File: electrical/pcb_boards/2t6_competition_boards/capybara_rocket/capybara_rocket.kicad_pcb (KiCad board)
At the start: 4 copper layers, 160 x 65 mm, 121 parts, among them J1 3.6V Battery, J10 Elevator, J11 SparkFun MAX-M10S, J12 Aileron 1, J13 Aileron 2, J14 Ground Camera, J15 Payload Camera, J16 DC Motor, J2 1.2V Battery, J3 3.6V Switch, J4 1.2V Switch, J5 LED, J6 NC, J7 CC, J8 VL53L1-SATEL, J9 Egg, Q1 SI4435DDY, Q2 SI4435DDY, U1 DS1307+, U10 TPS3839, U11 MP3414, U12 SN74LVC1G04, U13 MCP1640, U14 TPS3839, U15 STM32 NUCLEO-G431KB, U16 SN74AUP1G04, U17 SparkFun XBee Explorer, U2 Adafruit BNO085, U3 TLC555, U4 EEPROM, U5 LTC3536, U6 LTC3536, U7 Adafruit BMP581, U8 DRV8212, U9 INA219, Y1 AB38T-32.768KHZ

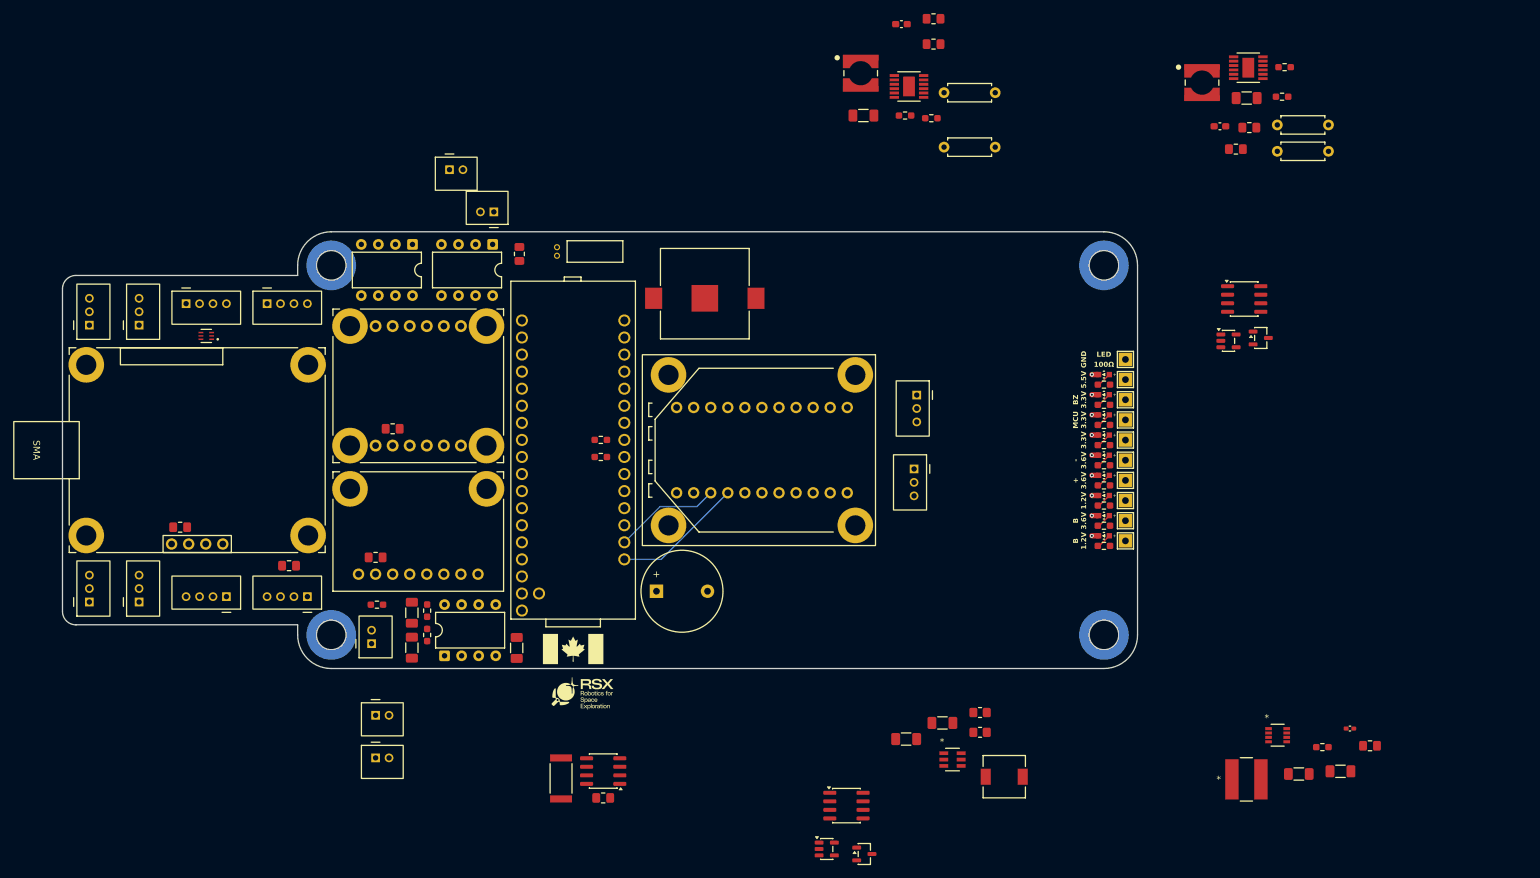
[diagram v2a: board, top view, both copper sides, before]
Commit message: Completed layout for CPL PCB
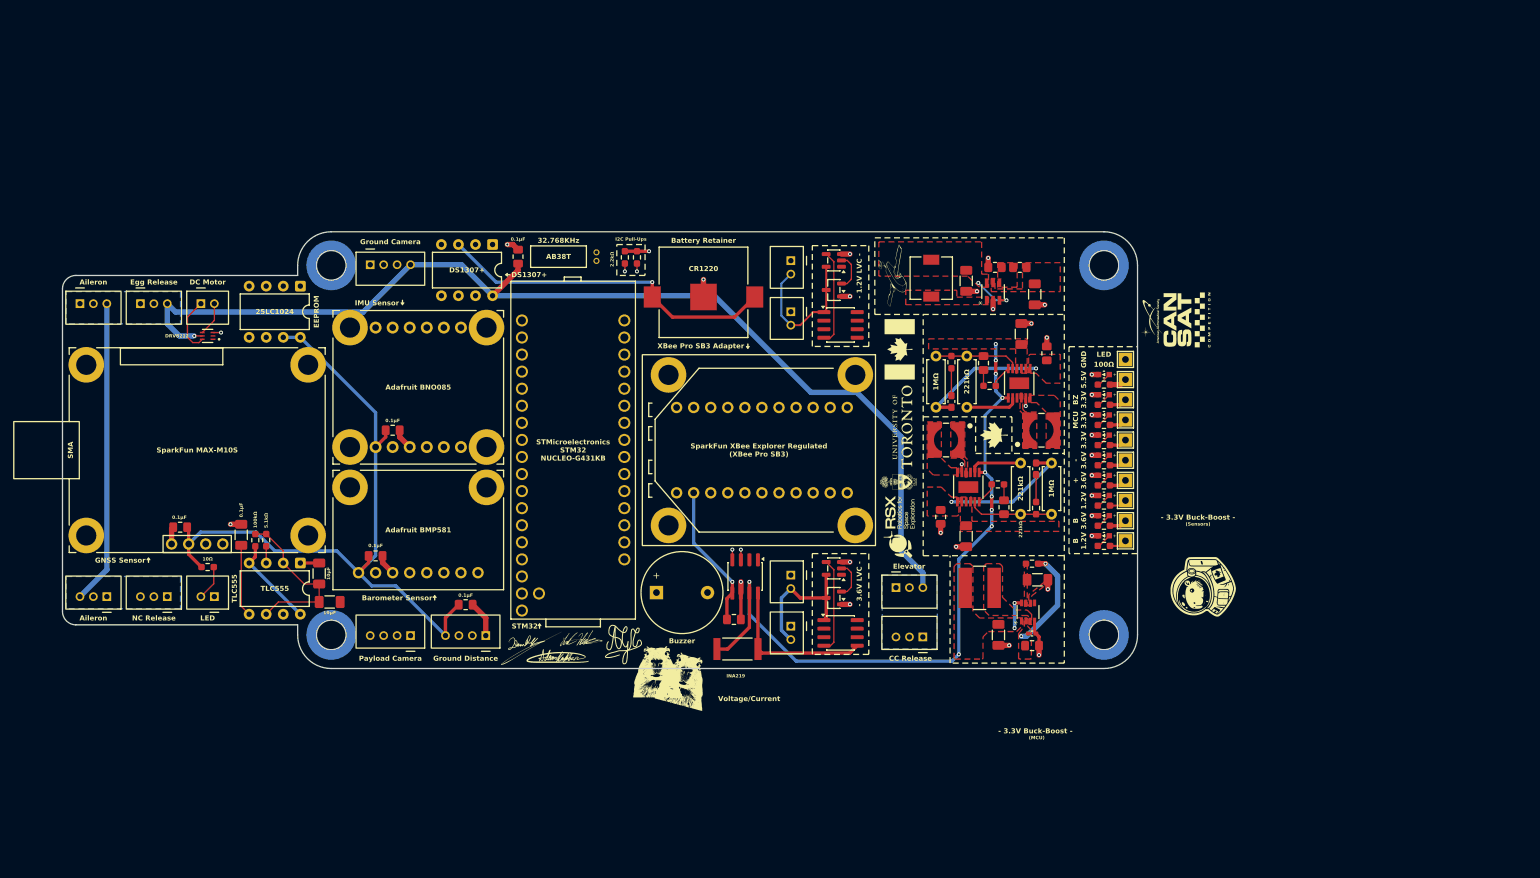
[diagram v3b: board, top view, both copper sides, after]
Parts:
- added ?: , clipboard:8695c1bd-c6c1-4d98-8ee2-76d7a5019fa7, F.Cu at (125.4, 121.6)
- added ?: , clipboard:8695c1bd-c6c1-4d98-8ee2-76d7a5019fa7, F.Cu at (135.9, 73.9)
- added ?: , clipboard:8695c1bd-c6c1-4d98-8ee2-76d7a5019fa7, F.Cu at (141.0, 125.8)
- added ?: , clipboard:8695c1bd-c6c1-4d98-8ee2-76d7a5019fa7, F.Cu at (172.0, 84.9)
- added ?: , clipboard:8695c1bd-c6c1-4d98-8ee2-76d7a5019fa7, F.Cu at (82.8, 116.0)
- added ?: , clipboard:8695c1bd-c6c1-4d98-8ee2-76d7a5019fa7, F.Cu at (120.6, 78.4)
- added G***: LOGO, LOGO, F.Cu at (139.8, 129.4)
- added G***: LOGO, LOGO, F.Cu at (153.6, 129.0)
- added G***: LOGO, RSX_CanSat_Graphics:maple_leaf, F.Cu at (208.6, 97.8)
- added G***: LOGO, RSX_CanSat_Graphics:capybara_astronaut_2, B.Cu at (93.6, 64.6)
- added G***: LOGO, CAN-RGX:uoft, F.Cu at (194.6, 98.2)
- added G***: LOGO, LOGO, F.Cu at (143.6, 130.8)
- added G***: LOGO, RSX_CanSat_Graphics:capybara, F.Cu at (162.7, 133.5)
- added G***: LOGO, RSX_CanSat_Graphics:capybara, F.Cu at (158.5, 132.3)
- added G***: LOGO, RSX_CanSat_Graphics:capybara_astronaut_2, F.Cu at (239.8, 120.2)
- added G***: LOGO, LOGO, F.Cu at (147.5, 127.5)
- added G***: LOGO, RSX_CanSat_Graphics:cansat_logo_2, F.Cu at (235.7, 80.6)
- added G***: LOGO, LOGO, F.Cu at (193.2, 74.0)
- J16: footprint RSX_CanSat_Custom_KiCad_Footprints:J_Wurth_WR-WTB_62000411622 -> RSX_CanSat_Custom_KiCad_Footprints:J_Wurth_WR-WTB_62000211622
- moved J2 91.6 mm to (178.4, 71.8), turned to -90 degrees
- moved J4 90.7 mm to (178.4, 79.4), turned to -90 degrees
- moved U16 87.6 mm to (184.8, 71.8), turned to 180 degrees
- moved J1 84.8 mm to (178.4, 126.2), turned to -90 degrees
- moved U14 84.1 mm to (184.8, 76.2), turned to 180 degrees
- moved Q1 78.0 mm to (185.8, 127.2)
- moved C7 77.4 mm to (204.5, 112.8), turned to -90 degrees
- moved R5 75.3 mm to (209.2, 105.1)
- moved U6 75.0 mm to (204.8, 105.5), turned to -90 degrees
- moved L4 75.0 mm to (199.3, 74.4), turned to 90 degrees
- moved U10 74.4 mm to (184.8, 122.0), turned to 180 degrees
- moved C17 73.9 mm to (200.7, 109.9), turned to 90 degrees
- moved Q2 71.5 mm to (185.8, 81.4)
- moved R8 71.3 mm to (214.9, 108.6), turned to 90 degrees
- moved U13 69.9 mm to (208.5, 76.4), turned to 90 degrees
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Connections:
- J16 pad 1: GND -> DC_PWM_1
- J16 pad 2: DC_PWM_1 -> DC_PWM_2
- J8 pad 2: SCL -> SDA
- J8 pad 3: SDA -> SCL
- U5 pad 8: unconnected-(U5-VIN_2-Pad8) -> 3.6V-
- U6 pad 8: unconnected-(U6-VIN_2-Pad8) -> 3.6V-
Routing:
- net 5.5V: track 0.00 -> 225.5 mm, vias 0 -> 3
- net 3.3V: track 0.00 -> 154.4 mm, vias 0 -> 3
- net 3.6V-: track 0.00 -> 111.5 mm, vias 0 -> 12
- net GND: track 9.00 -> 82.0 mm, vias 9 -> 31
- net SDA: track 0.00 -> 61.5 mm, vias 0 -> 2
- net SCL: track 0.00 -> 60.7 mm, vias 0 -> 2
- net Net-(U1-VBAT): track 0.00 -> 51.1 mm, vias 0 -> 1
- net AILERON: track 0.00 -> 46.4 mm
- net 3.6V+: track 0.00 -> 26.4 mm
- net Net-(U3-THRES): track 0.00 -> 24.9 mm
- net 3.6V B: track 0.00 -> 24.1 mm
- net 1.2V B: track 0.00 -> 24.0 mm
- net 3.3V MCU: track 0.00 -> 22.2 mm, vias 0 -> 1
- net X2: track 0.00 -> 19.0 mm
- net 3.3V BZ: track 0.00 -> 16.2 mm
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- added copper zone on F.Cu, net 1.2V
- added copper zone on F.Cu, net 3.3V
- added copper zone on F.Cu, net 3.3V BZ
- added copper zone on F.Cu, net 3.3V MCU
- added copper zone on F.Cu, net 3.6V-
- added copper zone on B.Cu, net 5.5V
- added copper zone on F.Cu, net 5.5V
- added copper zone on F.Cu, net GND
- added copper zone on F.Cu, net Net-(U11-FB)
- added copper zone on F.Cu, net Net-(U11-SW)
- added copper zone on F.Cu, net Net-(U13-SW)
- added copper zone on F.Cu, net Net-(U13-VFB)
- added copper zone on F.Cu, net Net-(U5-SW1)
- added copper zone on F.Cu, net Net-(U5-SW2)
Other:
- board text added: "(+)"
- board text added: "(MCU)"
- board text added: "(Sensors)"
- board text added: "- 1.2V LVC -"
- board text added: "- 3.3V Buck-Boost -"
- board text added: "- 3.6V LVC -"
- board text added: "0.1μF"
- board text added: "100kΩ"
- board text added: "10Ω"
- board text added: "10μF"
- board text added: "1MΩ"
- board text added: "2.2kΩ"
- board text added: "221kΩ"
- board text added: "25LC1024"
- board text added: "32.768KHz"
- board text added: "3Vo"
- board text added: "5.1kΩ"
- board text added: "AB38T"
- board text added: "Adafruit BMP581"
- board text added: "Adafruit BNO085"
- board text added: "Adam Kabbara Arthur Goetzke-Coburn Daniel Yu Luke Watson Angelique Liao Ada Selcuk Yulin Lin Jingshu Zhu Vincent Jia Wareesha Qureshi Parth Bhasin John Yfantis Nathan Xia Gianluca Ceccacci Berk Yilmaz Remi Zhang June 4-7, 2026 Monterey, Virginia United States"
- board text added: "Aileron"
- board text added: "BT"
- board text added: "Barometer Sensor"
- board text added: "Battery Retainer"
- board text added: "Buzzer"
- board text added: "CC Release"
- board text added: "CONT"
- board text added: "CR1220"
- board text added: "CS"
- board text added: "DC Motor"
- board text added: "DI"
- board text added: "DISCH"
- board text added: "DRV8212"
- board text added: "DS1307+"
- board text added: "EEPROM"
- board text added: "EGG_REL"
- board text added: "Egg Release"
- board text added: "Elevator"
- board text added: "GNSS Sensor"
- board text added: "Ground Camera"
- board text added: "Ground Distance"
- board text added: "HOLD"
- board text added: "I2C Pull-Ups"
- board text added: "IMU Sensor"
- board text added: "INA219"
- board text added: "INT"
- board text added: "MISO"
- board text added: "MOSI"
- board text added: "NC Release"
- board text added: "OUT"
- board text added: "P0"
- board text added: "P1"
- board text added: "Payload Camera"
- board text added: "RST"
- board text added: "SCLK"
- board text added: "SDO"
- board text added: "STM32"
- board text added: "STMicroelectronics STM32 NUCLEO-G431KB"
- board text added: "SparkFun MAX-M10S"
- board text added: "SparkFun XBee Explorer Regulated (XBee Pro SB3)"
- board text added: "THRES"
- board text added: "TLC555"
- board text added: "TRIG"
- board text added: "VCC"
- board text added: "VIN"
- board text added: "VSS"
- board text added: "Voltage/Current"
- board text added: "WP"
- board text added: "X1"
- board text added: "X2"
- board text added: "XBee Pro SB3 Adapter"
- board text removed: "Adam Kabbara Arthur Goetzke-Coburn Daniel Yu Luke Watson Angelique Liao Ada Selcuk Yulin Lin Jingshu Zhu Vincent Jia Wareesha Qureshi Parth Bhasin John Yfantis Nathan Xia Gianluca Ceccacci Berk Yilmaz Remi Zhang"
- board text removed: "EGG"

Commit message: Left side of the board done :)
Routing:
- net Net-(BZ1-+): track 2.49 -> 66.5 mm, vias 0 -> 2
- net PG_CAM_OUT: track 0.00 -> 8.26 mm, vias 0 -> 1
- net PG_CAM_IN: track 0.00 -> 5.93 mm, vias 0 -> 1
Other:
- board text added: "VBAT"
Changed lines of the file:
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@@
+		)
+	)
+	(gr_text "OUT"
+		(at 131.47 78.2 90)
+		(layer "B.SilkS")
+		(effects
+			(font
+				(size 0.75 0.75)
+				(thickness 0.125)
+				(bold yes)
+			)
+			(justify left mirror)
+		)
+	)
+	(gr_text "VBAT"
+		(at 128.93 70.6 90)
+		(layer "B.SilkS")
+		(effects
+			(font
+				(size 0.75 0.75)
+				(thickness 0.125)
+				(bold yes)
+			)
+			(justify left mirror)
 		)
 	)
@@
 		)
 	)
+	(gr_text "SCL"
+		(at 128.93 78.2 90)
+		(layer "B.SilkS")
+		(effects
+			(font
+				(size 0.75 0.75)
+				(thickness 0.125)
+				(bold yes)
+			)
+			(justify left mirror)
+		)
+	)
 	(gr_text "WP"
 		(at 100.32 76.8 90)
@@
 		)
 	)
+	(gr_text "X2"
+		(at 131.47 70.6 90)
+		(layer "B.SilkS")
+		(effects
+			(font
+				(size 0.75 0.75)
+				(thickness 0.125)
+				(bold yes)
+			)
+			(justify left mirror)
+		)
+	)
 	(gr_text "5.5V"
 		(at 115.8 126.6 90)
@@
 		)
 	)
+	(gr_text "GND"
+		(at 126.39 70.6 90)
+		(layer "B.SilkS")
+		(effects
+			(font
+				(size 0.75 0.75)
+				(thickness 0.125)
+				(bold yes)
+			)
+			(justify left mirror)
+		)
+	)
 	(gr_text "MCU\n3.3V"
 		(at 225.6 95.5 90)
@@
 		)
 	)
+	(gr_text "VCC"
+		(at 136 77 90)
+		(layer "B.SilkS")
+		(effects
+			(font
+				(size 0.75 0.75)
+				(thickness 0.125)
+				(bold yes)
+			)
+			(justify mirror)
+		)
+	)
 	(gr_text "SDA"
 		(at 126.76 98.1 90)
@@
 		)
 	)
+	(gr_text "X1"
+		(at 134.01 70.6 90)
+		(layer "B.SilkS")
+		(effects
+			(font
+				(size 0.75 0.75)
+				(thickness 0.125)
+				(bold yes)
+			)
+			(justify left mirror)
+		)
+	)
 	(gr_text "OUT"
 		(at 100.32 115.6 90)
@@
 		)
 	)
+	(gr_text "SDA"
+		(at 126.39 78.2 90)
+		(layer "B.SilkS")
+		(effects
+			(font
+				(size 0.75 0.75)
+				(thickness 0.125)
+				(bold yes)
+			)
+			(justify left mirror)
+		)
+	)
 	(segment
 		(start 157.78 77.2)
@@
 		(width 0.2)
 		(layer "F.Cu")
+		(net 2)
+	)
+	(via
+		(at 133.6 123.2)
+		(size 0.6)
+		(drill 0.3)
+		(layers "F.Cu" "B.Cu")
+		(net 2)
+	)
+	(via
+		(at 124.6 123.2)
+		(size 0.6)
+		(drill 0.3)
+		(layers "F.Cu" "B.Cu")
+		(net 2)
+	)
+	(segment
+		(start 124.6 123.2)
+		(end 133.6 123.2)
+		(width 0.2)
+		(layer "B.Cu")
+		(net 2)
+	)
+	(segment
+		(start 133.6 123.2)
+		(end 136.6 126.2)
+		(width 0.2)
+		(layer "In2.Cu")
+		(net 2)
+	)
+	(segment
+		(start 106.72 123.2)
+		(end 100.32 116.8)
+		(width 0.2)
+		(layer "In2.Cu")
+		(net 2)
+	)
+	(segment
+		(start 124.6 123.2)
+		(end 106.72 123.2)
+		(width 0.2)
+		(layer "In2.Cu")
+		(net 2)
+	)
+	(segment
+		(start 136.6 126.2)
+		(end 153.4 126.2)
+		(width 0.2)
+		(layer "In2.Cu")
+		(net 2)
+	)
+	(segment
+		(start 153.4 126.2)
+		(end 158.4 121.2)
+		(width 0.2)
+		(layer "In2.Cu")
 		(net 2)
 	)
@@
 		(net 17)
 	)
-	(segment
+	(via
+		(at 124.4 131.6)
+		(size 0.6)
+		(drill 0.3)
+		(layers "F.Cu" "B.Cu")
+		(free yes)
+		(net 20)
+	)
+	(segment
+		(start 117.8 127.6)
+		(end 121.8 131.6)
+		(width 0.2)
+		(layer "In2.Cu")
+		(net 20)
+	)
+	(segment
+		(start 121.8 131.6)
+		(end 124.4 131.6)
+		(width 0.2)
+		(layer "In2.Cu")
+		(net 20)
+	)
+	(via
+		(at 124.4 130.8)
+		(size 0.6)
+		(drill 0.3)
+		(layers "F.Cu" "B.Cu")
+		(free yes)
+		(net 21)
+	)
+	(segment
+		(start 123 130.8)
+		(end 124.4 130.8)
+		(width 0.2)
+		(layer "In2.Cu")
+		(net 21)
+	)
+	(segment
+		(start 119.8 127.6)
+		(end 123 130.8)
+		(width 0.2)
+		(layer "In2.Cu")
+		(net 21)
+	)
+	(segment

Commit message: i used to pray for times like this
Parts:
- removed the G*** at (78.4, 137.9)
- removed the G*** at (80.2, 67.8)
- removed the G*** at (162.7, 133.5)
- removed the G*** at (158.5, 132.3)
- removed the G*** at (239.8, 120.2)
- removed the G*** at (235.7, 80.6)
- added ?: , clipboard:93b123cf-2e48-43e5-9063-7d4b21d145b6, B.Cu at (205.6, 93.1)
- added ?: , clipboard:93b123cf-2e48-43e5-9063-7d4b21d145b6, B.Cu at (218.2, 109.0)
- added ?: , clipboard:93b123cf-2e48-43e5-9063-7d4b21d145b6, B.Cu at (213.6, 109.0)
- added ?: , clipboard:93b123cf-2e48-43e5-9063-7d4b21d145b6, B.Cu at (201.0, 93.1)
- added G***: LOGO, LOGO, F.Cu at (224.6, 120.4)
- added G***: LOGO, LOGO, F.Cu at (164.3, 131.2)
- added G***: LOGO, LOGO, B.Cu at (202.9, 75.7)
- added G***: LOGO, LOGO, B.Cu at (121.6, 88.0)
- added G***: LOGO, LOGO, B.Cu at (152.3, 127.2)
- added G***: LOGO, LOGO, B.Cu at (129.6, 89.3)
- added G***: LOGO, LOGO, F.Cu at (156.1, 131.5)
- added G***: LOGO, LOGO, B.Cu at (113.6, 90.0)
- added G***: LOGO, LOGO, B.Cu at (174.9, 119.6)
- added G***: LOGO, RSX_CanSat_Graphics:skule, B.Cu at (213.2, 119.4)
- added G***: LOGO, LOGO, B.Cu at (199.5, 102.6)
- added G***: LOGO, LOGO, B.Cu at (175.2, 127.0)
- added G***: LOGO, LOGO, B.Cu at (162.5, 77.4)
- added G***: LOGO, LOGO, B.Cu at (175.2, 72.8)
- added G***: LOGO, LOGO, B.Cu at (174.9, 80.4)
- added G***: LOGO, LOGO, B.Cu at (125.6, 92.5)
- added G***: LOGO, LOGO, F.Cu at (224.6, 79.2)
- added G***: LOGO, LOGO, F.Cu at (158.6, 130.1)
- added G***: LOGO, LOGO, F.Cu at (161.6, 131.0)
- moved G*** 52.3 mm to (123.4, 107.6), turned to 180 degrees
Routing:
- net 3.3V BZ: track 16.2 -> 195.8 mm, vias 0 -> 6
- net 3.3V: track 154.4 -> 312.0 mm, vias 3 -> 11
- net SDA: track 61.5 -> 201.4 mm, vias 2 -> 6
- net SCL: track 60.7 -> 188.5 mm
- net 5.5V: track 225.5 -> 347.8 mm, vias 3 -> 7
- net AILERON: track 46.4 -> 130.2 mm, vias 0 -> 1
- net 3.3V MCU: track 22.2 -> 105.4 mm, vias 1 -> 4
- net EGG_REL: track 0.00 -> 81.4 mm, vias 0 -> 2
- net NC_REL: track 0.00 -> 76.5 mm, vias 0 -> 2
- net CC_REL: track 0.00 -> 76.0 mm, vias 0 -> 1
- net 1.2V B: track 24.0 -> 99.0 mm, vias 0 -> 4
- net ELEVATOR: track 0.00 -> 71.1 mm, vias 0 -> 1
- net 3.6V B: track 24.1 -> 86.9 mm, vias 0 -> 3
- net PG_CAM_IN: track 5.93 -> 67.3 mm
- net PG_CAM_OUT: track 8.26 -> 67.4 mm
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- added copper zone on F.Cu, net Net-(U6-SW1)
- added copper zone on F.Cu, net Net-(U6-SW2)
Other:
- board text added: "+3V3"
- board text added: "+5V"
- board text added: "- 3.3V Boost -"
- board text added: "- 5.5V Boost -"
- board text added: "0.1Ω"
- board text added: "1.2V B"
- board text added: "1.2V Battery & Switch"
- board text added: "15μH"
- board text added: "1μF"
- board text added: "2.2μH"
- board text added: "220pF"
- board text added: "22μF"
- board text added: "3.6V B"
- board text added: "3.6V Battery & Switch"
- board text added: "4.7μH"
- board text added: "47pF"
- board text added: "505kΩ"
- board text added: "51kΩ"
- board text added: "562kΩ"
- board text added: "5V"
- board text added: "6.2kΩ"
- board text added: "61.9kΩ"
- board text added: "976kΩ"
- board text added: "AVDD"
- board text added: "Battery"
- board text added: "CC_REL"
- board text added: "CTS"
- board text added: "DIN"
- board text added: "DIO0"
- board text added: "DIO1"
- board text added: "DIO11"
- board text added: "DIO12"
- board text added: "DIO2"
- board text added: "DIO3"
- board text added: "DIO4"
- board text added: "DIO5"
- board text added: "DIO9"
- board text added: "DOUT"
- board text added: "DTR"
- board text added: "ELEVATOR"
- board text added: "GND_SWD"
- board text added: "LTC3536"
- board text added: "MCP1640"
- board text added: "MP3414"
- board text added: "NRST"
- board text added: "PA0"
- board text added: "PA1"
- board text added: "PA10"
- board text added: "PA11"
- board text added: "PA12"
- board text added: "PA15"
- board text added: "PA2"
- board text added: "PA3"
- board text added: "PA4"
- board text added: "PA5/PB7"
- board text added: "PA6/PA15"
- board text added: "PA7"
- board text added: "PA8"
- board text added: "PA9"
- board text added: "PB0"
- board text added: "PB3/PB8"
- board text added: "PB4"
- board text added: "PB5"
- board text added: "PB6"
- board text added: "PB7"
- board text added: "PF0"
- board text added: "PF1"
- board text added: "PT2512FK"
- board text added: "RES1"
- board text added: "RES2"
- board text added: "RSSI"
- board text added: "RSX Aerial CanSat 2T5-2T6 Team"
- board text added: "RTS"
- board text added: "SI4435DDY"
- board text added: "SWCLK"
- board text added: "SWDIO"
- board text added: "Switch"
- board text added: "V/A"
- board text removed: "RSX Aerial CanSat 2T5-2T6"
- board text removed: "Voltage/Current"

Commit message: i used to pray for times like this pt2
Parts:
- added G***: LOGO, LOGO, B.Cu at (213.7, 93.3)
